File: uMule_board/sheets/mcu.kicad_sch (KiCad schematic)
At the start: 23 parts, among them SW1 DBG_BUTT, SW2 RST, U5 STM32F103RCTx, U6 FM24C64B, Y1 8MHz

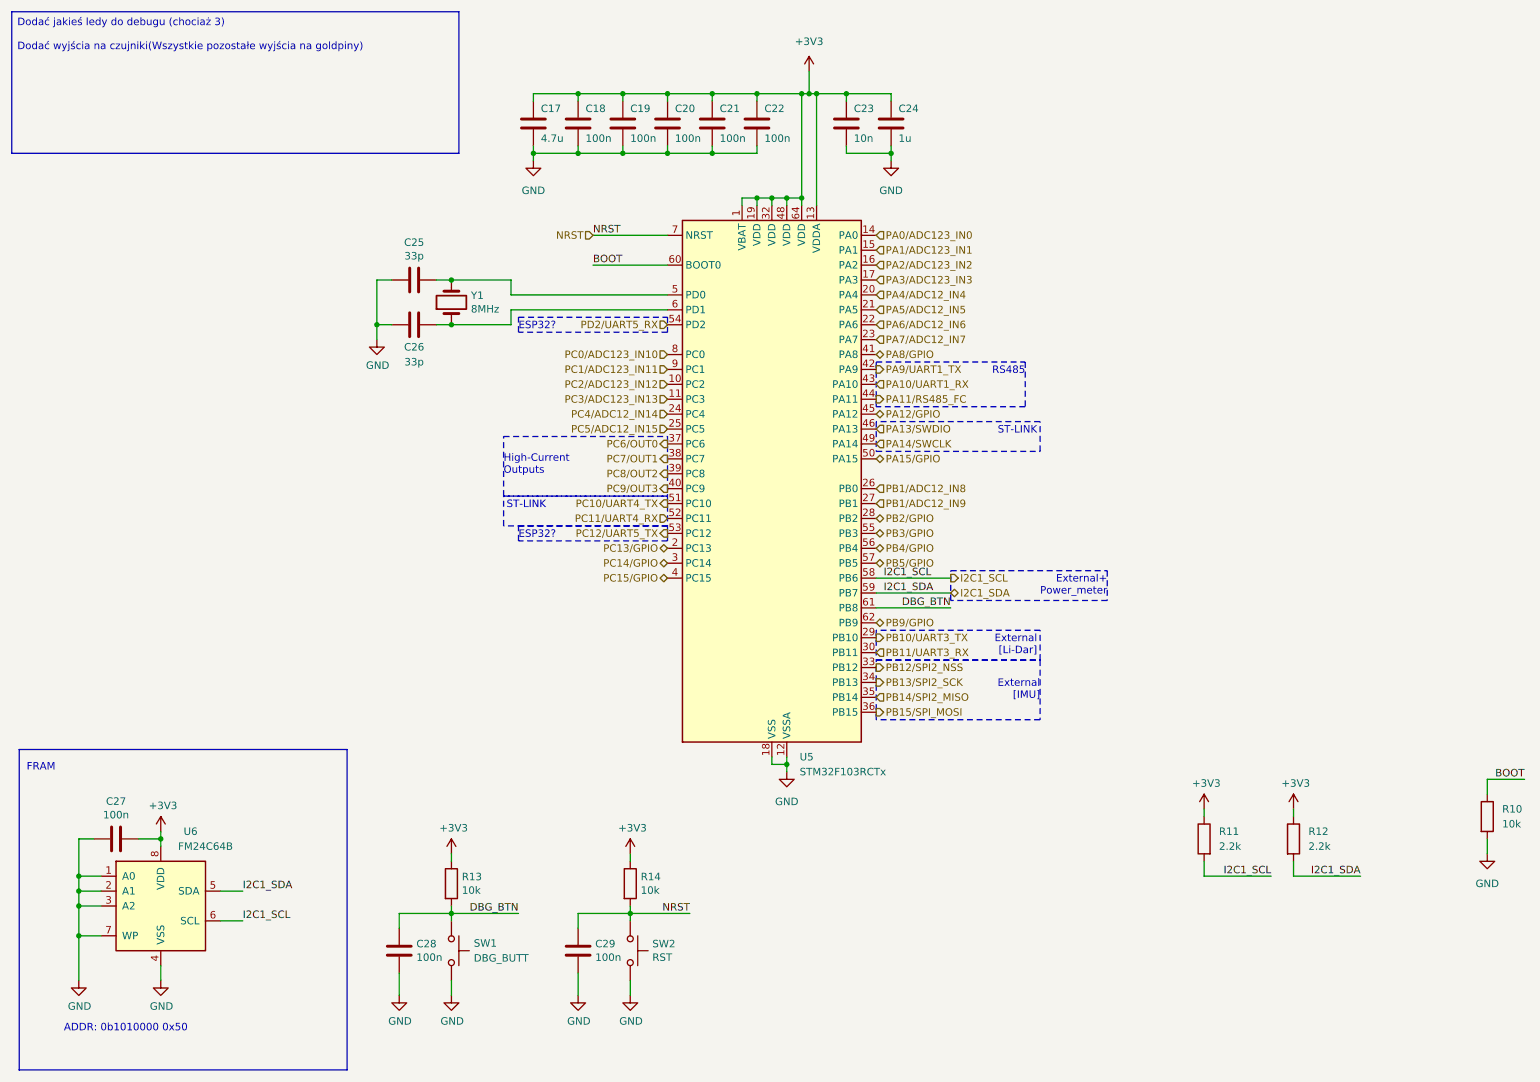
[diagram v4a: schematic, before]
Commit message: Started working on PCB. Ditched high power outputs. Focusing on photodiodes. One commit closer to order
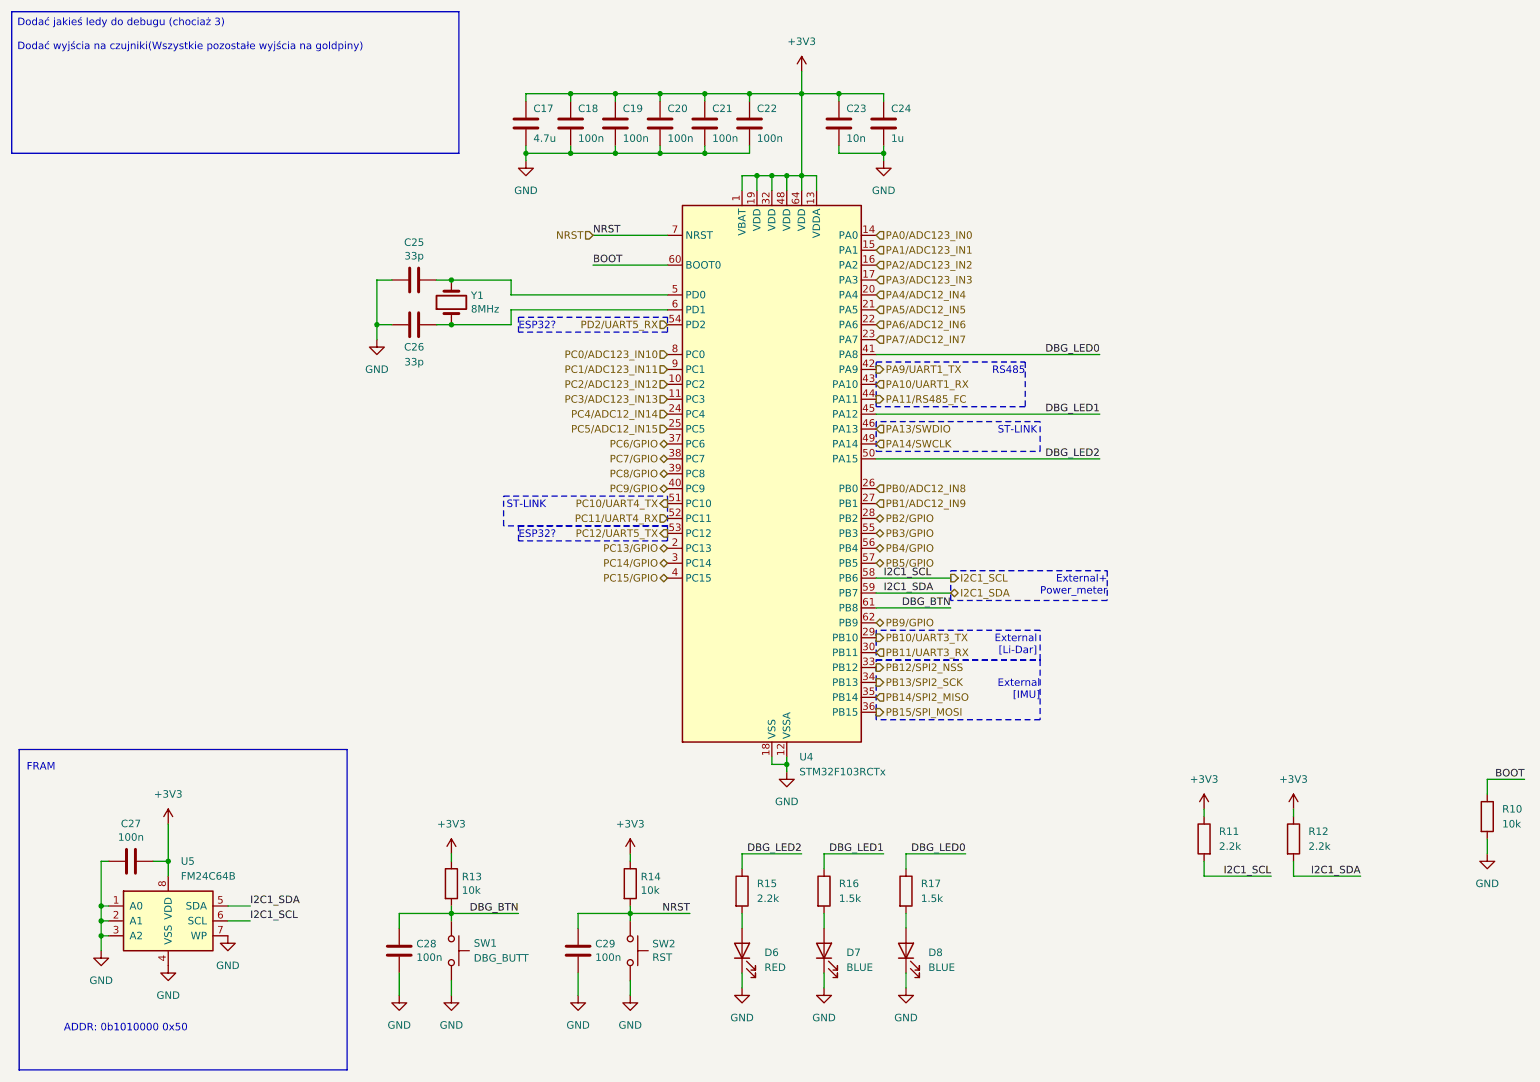
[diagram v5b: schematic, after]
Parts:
- removed U5: STM32F103RCTx, Package_QFP:LQFP-64_10x10mm_P0.5mm, symbol MCU_ST_STM32F1:STM32F103RCTx
- removed U6: FM24C64B, Package_SO:SOIC-8_3.9x4.9mm_P1.27mm, symbol Memory_NVRAM:FM24C64B
- added D6: RED, LED_SMD:LED_0603_1608Metric_Pad1.05x0.95mm_HandSolder, symbol Device:LED
- added D7, D8: BLUE, LED_SMD:LED_0603_1608Metric_Pad1.05x0.95mm_HandSolder, symbol Device:LED
- added R15: 2.2k, Resistor_SMD:R_0603_1608Metric, symbol Device:R
- added R16, R17: 1.5k, Resistor_SMD:R_0603_1608Metric, symbol Device:R
- added U4: STM32F103RCTx, Package_QFP:LQFP-64_10x10mm_P0.5mm, symbol MCU_ST_STM32F1:STM32F103RCTx
- added U5: FM24C64B, Package_SO:SOIC-8_3.9x4.9mm_P1.27mm, symbol Memory_NVRAM:FM24C64B
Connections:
- net +3V3: now also U4.1 (VBAT), U4.13 (VDDA), U4.19 (VDD), U4.32 (VDD), U4.48 (VDD), U4.64 (VDD), U5.8 (VDD)
- net BOOT: now also U4.60 (BOOT0)
- net DBG_BTN: now also U4.61 (PB8)
- net GND: now also D6.1 (K), D7.1 (K), D8.1 (K), U4.12 (VSSA), U4.18 (VSS), U4.31 (VSS), U4.47 (VSS), U4.63 (VSS), U5.1 (A0), U5.2 (A1), U5.3 (A2), U5.4 (VSS), U5.7 (WP)
- net I2C1_SCL: now also U4.58 (PB6), U5.6 (SCL)
- net I2C1_SDA: now also U4.59 (PB7), U5.5 (SDA)
- net NRST: now also U4.7 (NRST)
- net PA0/ADC123_IN0: now also U4.14 (PA0)
- net PA10/UART1_RX: now also U4.43 (PA10)
- net PA11/RS485_FC: now also U4.44 (PA11)
- net PA13/SWDIO: now also U4.46 (PA13)
- net PA14/SWCLK: now also U4.49 (PA14)
- net PA1/ADC123_IN1: now also U4.15 (PA1)
- net PA2/ADC123_IN2: now also U4.16 (PA2)
- net PA3/ADC123_IN3: now also U4.17 (PA3)
- net PA4/ADC12_IN4: now also U4.20 (PA4)
- net PA5/ADC12_IN5: now also U4.21 (PA5)
- net PA6/ADC12_IN6: now also U4.22 (PA6)
- net PA7/ADC12_IN7: now also U4.23 (PA7)
- net PA9/UART1_TX: now also U4.42 (PA9)
- net PB10/UART3_TX: now also U4.29 (PB10)
- net PB11/UART3_RX: now also U4.30 (PB11)
- net PB12/SPI2_NSS: now also U4.33 (PB12)
- net PB13/SPI2_SCK: now also U4.34 (PB13)
- net PB14/SPI2_MISO: now also U4.35 (PB14)
- net PB15/SPI_MOSI: now also U4.36 (PB15)
- net PB1/ADC12_IN9: now also U4.27 (PB1)
- net PB2/GPIO: now also U4.28 (PB2)
- net PB3/GPIO: now also U4.55 (PB3)
- net PB4/GPIO: now also U4.56 (PB4)
- net PB5/GPIO: now also U4.57 (PB5)
- net PB9/GPIO: now also U4.62 (PB9)
- net PC0/ADC123_IN10: now also U4.8 (PC0)
- net PC10/UART4_TX: now also U4.51 (PC10)
- net PC11/UART4_RX: now also U4.52 (PC11)
- net PC12/UART5_TX: now also U4.53 (PC12)
- net PC13/GPIO: now also U4.2 (PC13)
- net PC14/GPIO: now also U4.3 (PC14)
- net PC15/GPIO: now also U4.4 (PC15)
- net PC1/ADC123_IN11: now also U4.9 (PC1)
- net PC2/ADC123_IN12: now also U4.10 (PC2)
- net PC3/ADC123_IN13: now also U4.11 (PC3)
- net PC4/ADC12_IN14: now also U4.24 (PC4)
- net PC5/ADC12_IN15: now also U4.25 (PC5)
- net PD2/UART5_RX: now also U4.54 (PD2)
- net at C25.1, Y1.2: now also U4.5 (PD0)
- net at C26.1, Y1.1: now also U4.6 (PD1)
- new net: D8.2 (A), R17.2
- new net: D7.2 (A), R16.2
- new net: D6.2 (A), R15.2
- new net DBG_LED0: R17.1, U4.41 (PA8)
- new net DBG_LED1: R16.1, U4.45 (PA12)
- new net DBG_LED2: R15.1, U4.50 (PA15)
- new net PB0/ADC12_IN8: U4.26 (PB0)
- new net PC6/GPIO: U4.37 (PC6)
- new net PC7/GPIO: U4.38 (PC7)
- new net PC8/GPIO: U4.39 (PC8)
- new net PC9/GPIO: U4.40 (PC9)
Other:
- note removed: "High-Current Outputs"
- title: (none) -> uMule_board
- moved on the sheet: C17, C18, C19, C20, C21, C22, C23, C24

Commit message: removed half phototransistors, etc.
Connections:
- net PB0/ADC12_IN8 renamed PB0/GPIO
- net PB1/ADC12_IN9 renamed PB1/GPIO
- net PC0/ADC123_IN10 renamed PC0/GPIO
- net PC1/ADC123_IN11 renamed PC1/GPIO
- net PC2/ADC123_IN12 renamed PC2/GPIO
- net PC3/ADC123_IN13 renamed PC3/GPIO
- net PC4/ADC12_IN14 renamed PC4/GPIO
- net PC5/ADC12_IN15 renamed PC5/GPIO
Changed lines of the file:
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@@
 		)
 	)
-	(hierarchical_label "PC1{slash}ADC123_IN11"
-		(shape input)
+	(hierarchical_label "PC1{slash}GPIO"
+		(shape bidirectional)
 		(at 125.73 74.93 180)
 		(effects
@@
 		)
 	)
-	(hierarchical_label "PC3{slash}ADC123_IN13"
-		(shape input)
+	(hierarchical_label "PC3{slash}GPIO"
+		(shape bidirectional)
 		(at 125.73 80.01 180)
 		(effects
@@
 		)
 	)
-	(hierarchical_label "PC2{slash}ADC123_IN12"
-		(shape input)
+	(hierarchical_label "PC2{slash}GPIO"
+		(shape bidirectional)
 		(at 125.73 77.47 180)
 		(effects
@@
 		)
 	)
-	(hierarchical_label "PC0{slash}ADC123_IN10"
-		(shape input)
+	(hierarchical_label "PC0{slash}GPIO"
+		(shape bidirectional)
 		(at 125.73 72.39 180)
 		(effects
@@
 		)
 	)
-	(hierarchical_label "PB1{slash}ADC12_IN9"
-		(shape input)
+	(hierarchical_label "PB1{slash}GPIO"
+		(shape bidirectional)
 		(at 161.29 97.79 0)
 		(effects
@@
 		)
 	)
-	(hierarchical_label "PC4{slash}ADC12_IN14"
-		(shape input)
+	(hierarchical_label "PC4{slash}GPIO"
+		(shape bidirectional)
 		(at 125.73 82.55 180)
 		(effects
@@
 		)
 	)
-	(hierarchical_label "PB0{slash}ADC12_IN8"
-		(shape input)
+	(hierarchical_label "PB0{slash}GPIO"
+		(shape bidirectional)
 		(at 161.29 95.25 0)
 		(effects
@@
 		)
 	)
-	(hierarchical_label "PC5{slash}ADC12_IN15"
-		(shape input)
+	(hierarchical_label "PC5{slash}GPIO"
+		(shape bidirectional)
 		(at 125.73 85.09 180)
 		(effects

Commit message: sch ready, only missing the pcb
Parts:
- renumbered C17 to C28, C18 to C29, C19 to C30, C20 to C31, C21 to C32, C22 to C33, C23 to C34, C24 to C35, C25 to C36, C26 to C37, C27 to C38, C28 to C39, C29 to C40, D8 to D10, D6 to D8, D7 to D9, R10 to R19, R11 to R20, R12 to R21, R13 to R22, R14 to R23, R15 to R24, R16 to R25, R17 to R26, U4 to U6, U5 to U7
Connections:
- net PB0/GPIO renamed PB0/ADC12_IN_REF

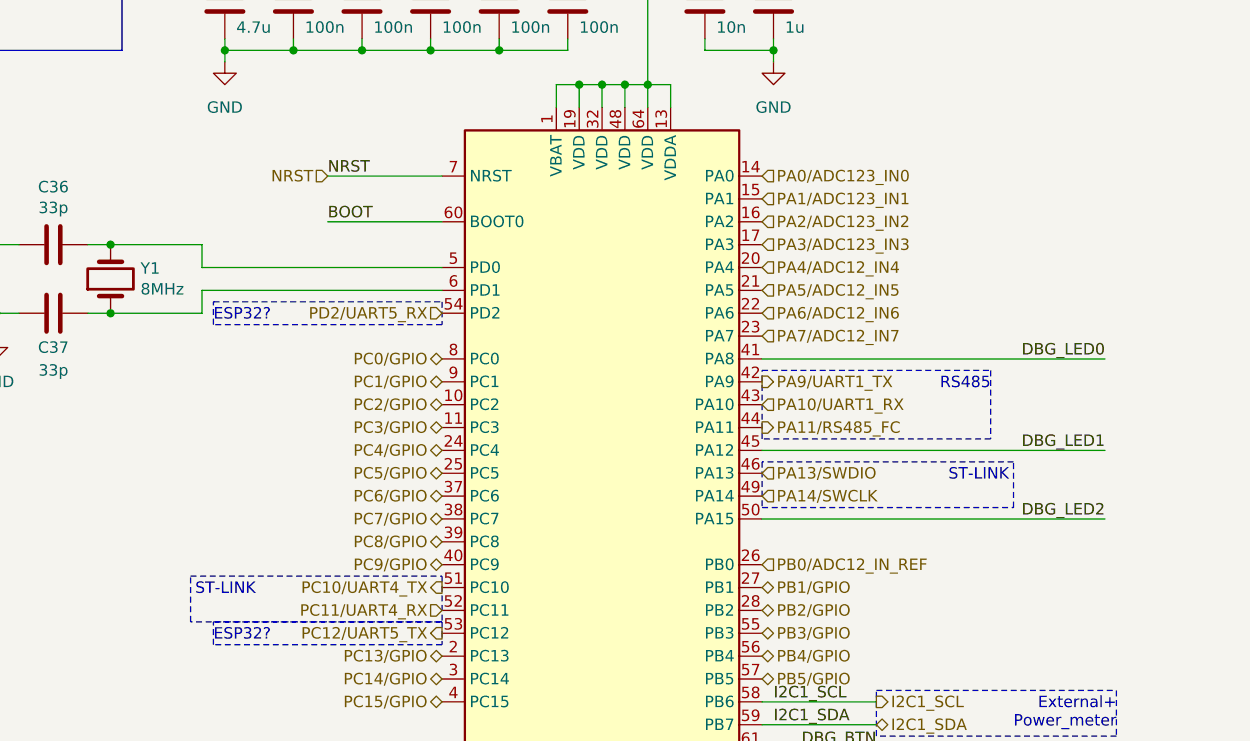
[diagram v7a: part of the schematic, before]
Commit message: another day, more progress. Elements are placed on board, traces need to be conected, added jumpers for power in case of bad design
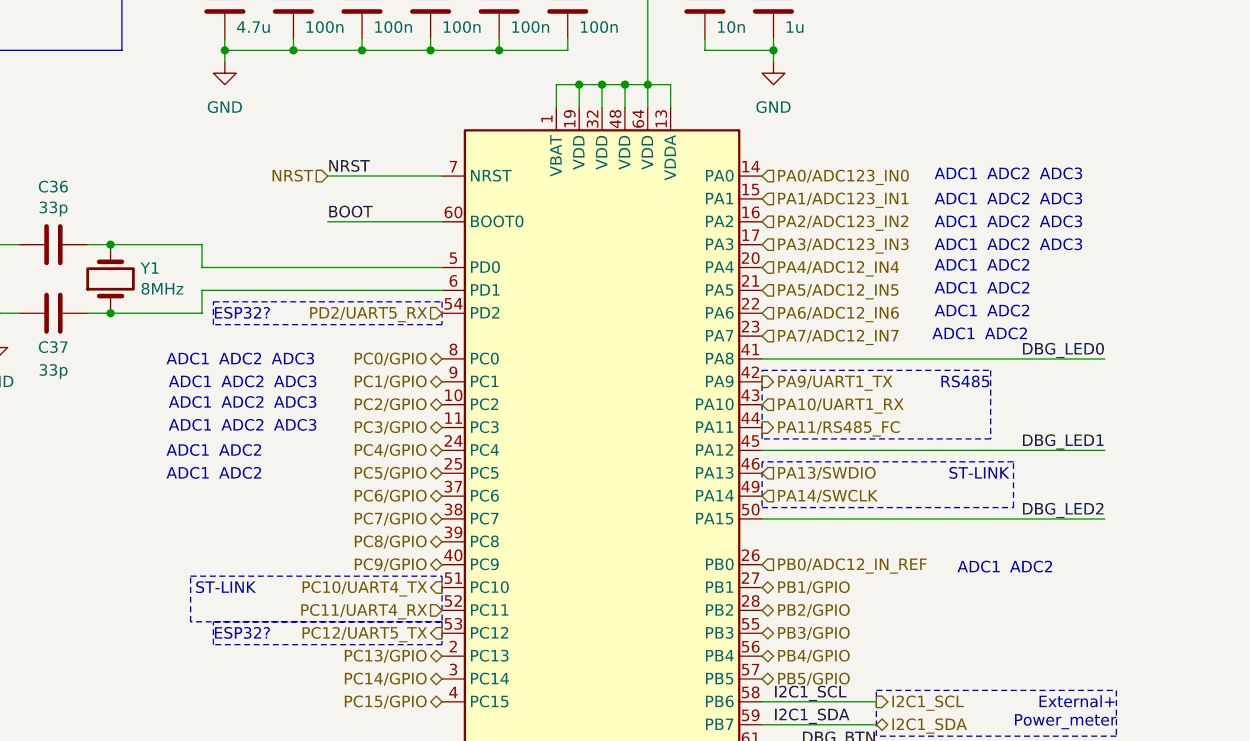
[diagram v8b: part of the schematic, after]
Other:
- note added: "ADC1"
- note added: "ADC2"
- note added: "ADC3"
